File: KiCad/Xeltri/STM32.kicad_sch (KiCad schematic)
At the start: 29 parts, among them U5 STM32H745XIHx

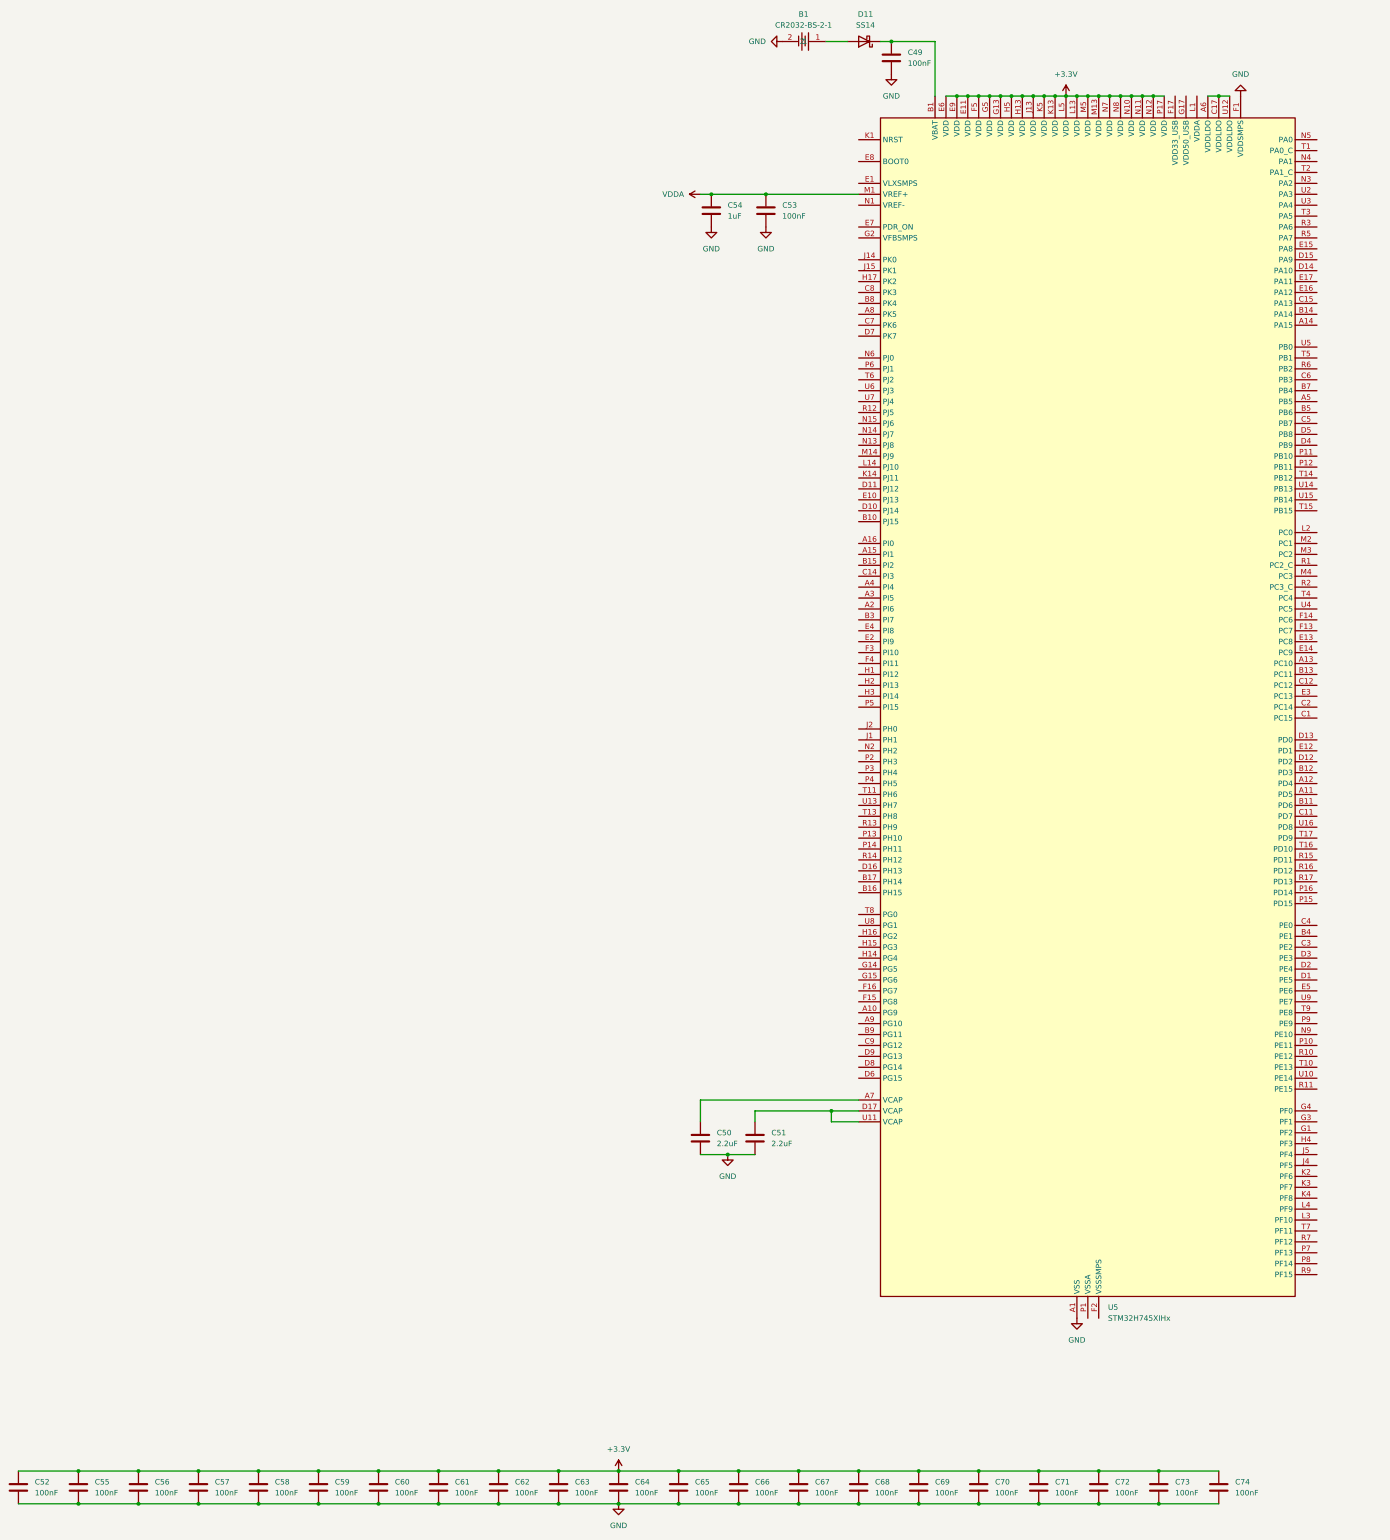
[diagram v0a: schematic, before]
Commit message: Rename the board to Xeltri and drop unused T113/old-selection files.
The KiCad project follows the rebrand; leftover T113 PDFs, the ESP32 stub, and unused HDMI/PMIC/inductor libraries are removed from the tree.

Co-authored-by: Cursor <cursoragent@cursor.com>
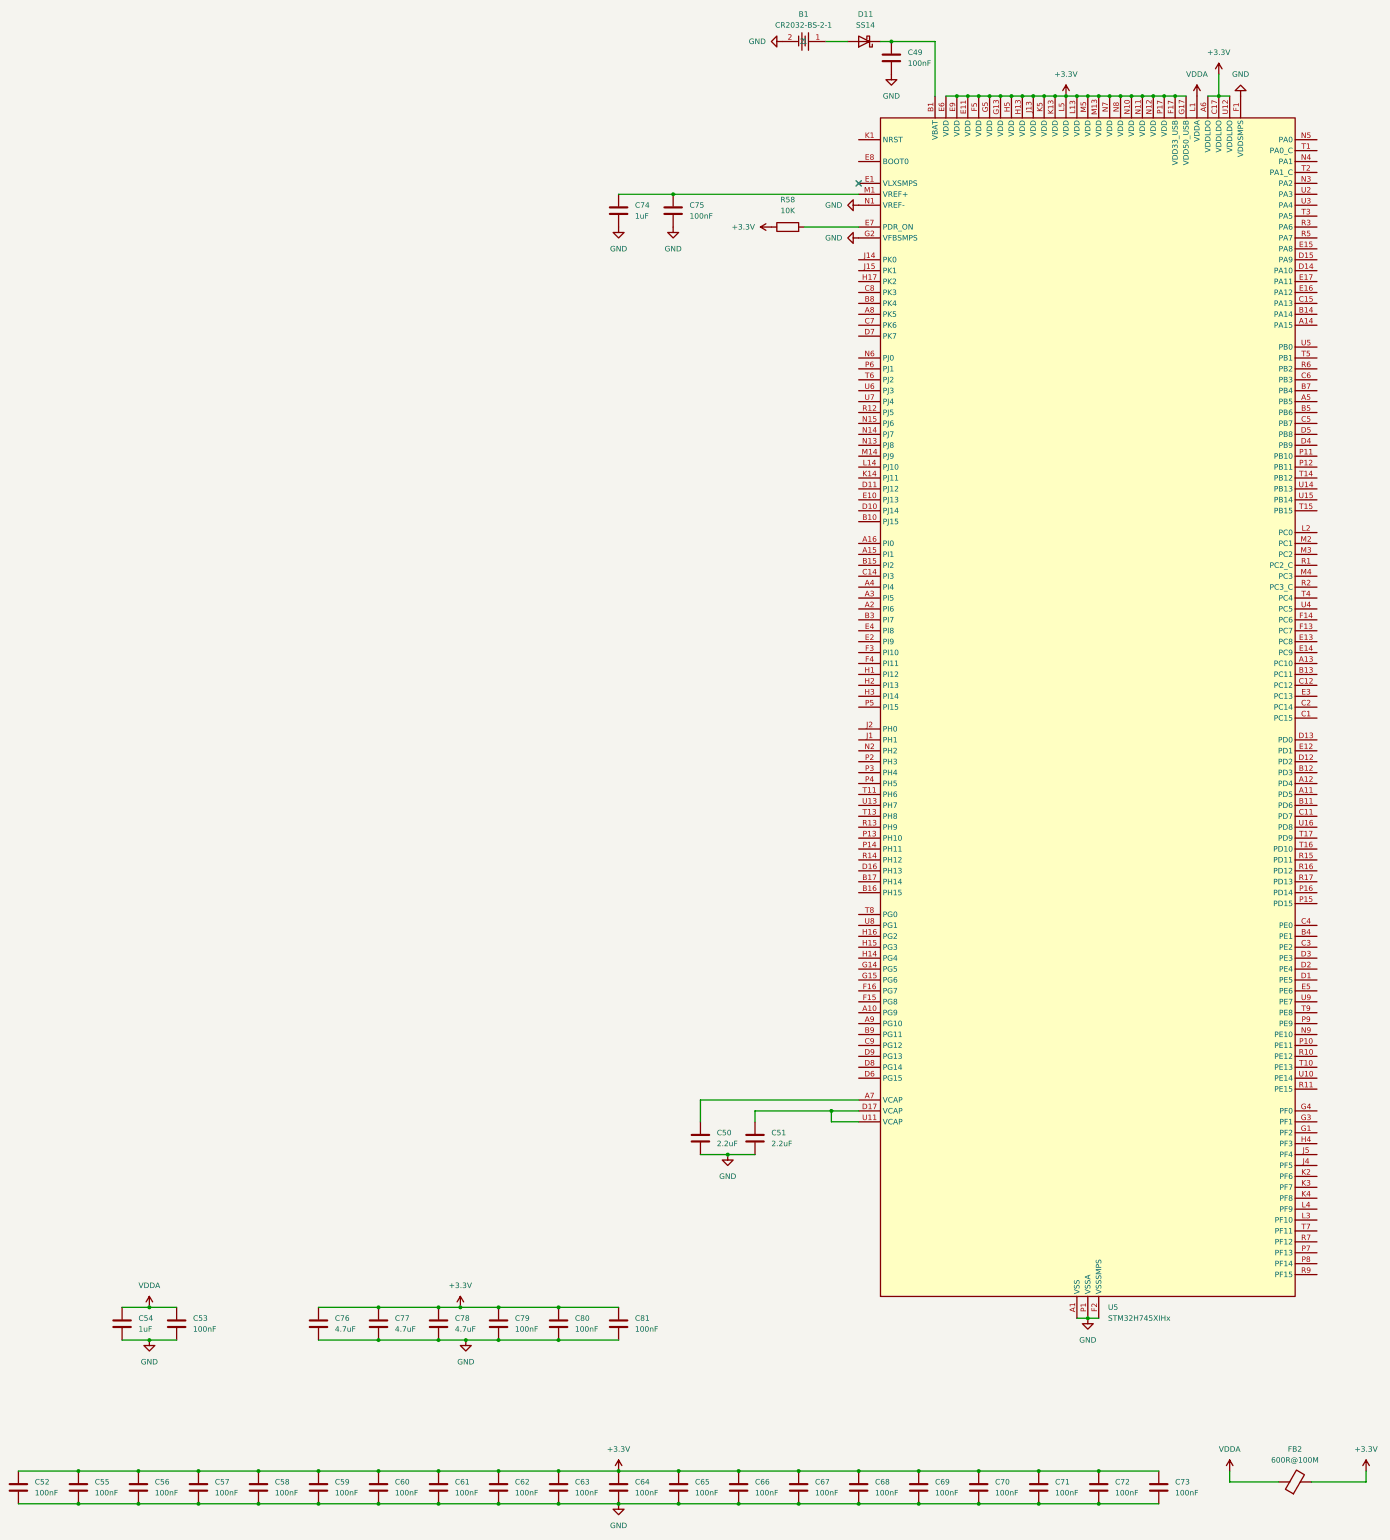
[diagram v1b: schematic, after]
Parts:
- added C75, C79, C80, C81: 100nF, Capacitor_SMD:C_0402_1005Metric, symbol Device:C
- added C76, C77, C78: 4.7uF, Capacitor_SMD:C_0805_2012Metric, symbol Device:C
- added FB2: 600R@100M, Inductor_SMD:L_0402_1005Metric, symbol Device:FerriteBead
- added R58: 10K, Resistor_SMD:R_0402_1005Metric, symbol Device:R
- C74: value 100nF -> 1uF
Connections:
- net +3.3V: now also U5.A6 (VDDLDO), U5.C17 (VDDLDO), U5.F17 (VDD33_USB), U5.G17 (VDD50_USB), U5.U12 (VDDLDO), C76.1, C77.1, C78.1, C79.1, C80.1, C81.1, FB2.2, R58.1; no longer C74.1
- net GND: now also U5.F2 (VSSSMPS), U5.G2 (VFBSMPS), U5.N1 (VREF-), U5.P1 (VSSA), C75.2, C76.2, C77.2, C78.2, C79.2, C80.2, C81.2
- net VDDA: now also U5.L1 (VDDA), FB2.1; no longer U5.M1 (VREF+)
- net at U5.E7 (PDR_ON): now also R58.2
- new net: C74.1, C75.1, U5.M1 (VREF+)
- no-connect marks 0 -> 1
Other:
- moved on the sheet: C53, C54
